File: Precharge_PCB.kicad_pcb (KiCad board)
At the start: 4 copper layers, 0 parts

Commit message: pcb: Setup net classes and import components
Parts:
- added C1: 22u, Capacitor_SMD:CP_Elec_6.3x7.7, F.Cu at (120.5, 110.7)
- added C10: 30p, Capacitor_SMD:C_0603_1608Metric, F.Cu at (76.6, 96.6)
- added C11: 100n, Capacitor_SMD:C_0603_1608Metric, F.Cu at (76.6, 99.1)
- added C12: 1u, Capacitor_SMD:C_0603_1608Metric, F.Cu at (76.6, 101.6)
- added C13: 100p, Capacitor_SMD:C_0603_1608Metric, F.Cu at (76.6, 104.1)
- added C14: 100p, Capacitor_SMD:C_0603_1608Metric, F.Cu at (76.6, 106.6)
- added C15: 1u, Capacitor_SMD:C_0603_1608Metric, F.Cu at (131.7, 124.9)
- added C16: 1u, Capacitor_SMD:C_0603_1608Metric, F.Cu at (131.7, 127.4)
- added C17: 1u, Capacitor_SMD:C_0603_1608Metric, F.Cu at (99.1, 118.7)
- added C18: 100n, Capacitor_SMD:C_0603_1608Metric, F.Cu at (99.1, 121.2)
- added C19: 1u, Capacitor_SMD:C_0603_1608Metric, F.Cu at (99.1, 123.7)
- added C2: 1u, Capacitor_SMD:C_0603_1608Metric, F.Cu at (72.6, 96.6)
- added C20: 100n, Capacitor_SMD:C_0603_1608Metric, F.Cu at (99.1, 126.2)
- added C21: 330p, Capacitor_SMD:C_0603_1608Metric, F.Cu at (99.1, 128.7)
- added C22: 330p, Capacitor_SMD:C_0603_1608Metric, F.Cu at (103.1, 118.7)
- added C23: 1u, Capacitor_SMD:C_0603_1608Metric, F.Cu at (103.1, 121.2)
- added C24: 1u, Capacitor_SMD:C_0603_1608Metric, F.Cu at (117.5, 118.7)
- added C25: 100n, Capacitor_SMD:C_0603_1608Metric, F.Cu at (117.5, 121.2)
- added C26: 1u, Capacitor_SMD:C_0603_1608Metric, F.Cu at (117.5, 123.7)
- added C27: 100n, Capacitor_SMD:C_0603_1608Metric, F.Cu at (117.5, 126.2)
- added C28: 330p, Capacitor_SMD:C_0603_1608Metric, F.Cu at (117.5, 128.7)
- added C29: 330p, Capacitor_SMD:C_0603_1608Metric, F.Cu at (121.5, 118.7)
- added C3: 1u, Capacitor_SMD:C_0603_1608Metric, F.Cu at (72.6, 99.1)
- added C30: 1u, Capacitor_SMD:C_0603_1608Metric, F.Cu at (121.5, 121.2)
- added C4: 1u, Capacitor_SMD:C_0603_1608Metric, F.Cu at (72.6, 101.6)
- added C5: 1u, Capacitor_SMD:C_0603_1608Metric, F.Cu at (72.6, 104.1)
- added C6: 1u, Capacitor_SMD:C_0603_1608Metric, F.Cu at (72.6, 106.6)
- added C7: 1u, Capacitor_SMD:C_0603_1608Metric, F.Cu at (72.6, 109.1)
- added C8: 1u, Capacitor_SMD:C_0603_1608Metric, F.Cu at (72.6, 111.6)
- added C9: 30p, Capacitor_SMD:C_0603_1608Metric, F.Cu at (72.6, 114.1)
- added D1: LED_Small, LED_SMD:LED_0603_1608Metric, F.Cu at (109.0, 64.9)
- added D10: LED_Small, LED_SMD:LED_0603_1608Metric, F.Cu at (113.1, 64.9)
- added D11: LED_Small, LED_SMD:LED_0603_1608Metric, F.Cu at (113.1, 67.5)
- added D12: LED_Small, LED_SMD:LED_0603_1608Metric, F.Cu at (113.1, 70.1)
- added D13: LED_Small, LED_SMD:LED_0603_1608Metric, F.Cu at (113.1, 72.7)
- added D14: LED_Small, LED_SMD:LED_0603_1608Metric, F.Cu at (113.1, 75.3)
- added D15: PESD2CAN, Package_TO_SOT_SMD:SOT-23, F.Cu at (93.4, 97.5)
- added D16: 1N4007, Diode_SMD:D_SMA, F.Cu at (103.0, 70.5)
- added D17: 1N4007, Diode_SMD:D_SMA, F.Cu at (103.0, 75.0)
- added D18: 3V6, Diode_SMD:D_SOD-323, F.Cu at (98.0, 112.2)
- added D19: 1N4007, Diode_SMD:D_SMA, F.Cu at (74.6, 132.4)
- added D2: SMAJ24CA, Diode_SMD:D_SMA, F.Cu at (103.0, 65.9)
- added D20: 1N4007, Diode_SMD:D_SMA, F.Cu at (159.0, 128.9)
- added D21: 1N4007, Diode_SMD:D_SMA, F.Cu at (133.8, 105.0)
- added D22: 1N4007, Diode_SMD:D_SMA, F.Cu at (133.8, 109.6)
- added D3: D_Schottky, Diode_SMD:D_SOD-323, F.Cu at (98.0, 103.4)
- added D4: D_Schottky, Diode_SMD:D_SOD-323, F.Cu at (98.0, 106.3)
- added D5: D_Schottky, Diode_SMD:D_SOD-323, F.Cu at (98.0, 109.3)
- added D6: LED_Small, LED_SMD:LED_0603_1608Metric, F.Cu at (109.0, 67.5)
- added D7: LED_Small, LED_SMD:LED_0603_1608Metric, F.Cu at (109.0, 70.1)
- added D8: LED_Small, LED_SMD:LED_0603_1608Metric, F.Cu at (109.0, 72.7)
- added D9: LED_Small, LED_SMD:LED_0603_1608Metric, F.Cu at (109.0, 75.3)
- added F1: Polyfuse, Capacitor_SMD:C_0805_2012Metric, F.Cu at (93.2, 113.7)
- added H1: MountingHole, MountingHole:MountingHole_3.2mm_M3, F.Cu at (111.3, 86.5)
- added H2: MountingHole, MountingHole:MountingHole_3.2mm_M3, F.Cu at (111.3, 94.5)
- added H3: MountingHole, MountingHole:MountingHole_3.2mm_M3, F.Cu at (111.3, 102.4)
- added H4: MountingHole, MountingHole:MountingHole_3.2mm_M3, F.Cu at (111.3, 110.4)
- added J1: Conn_01x02, yfs:MolexMicrofitPlus1x2, F.Cu at (76.3, 85.6)
- added J2: Conn_01x02, yfs:MolexMicrofitPlus1x2, F.Cu at (85.5, 85.6)
- added J3: Conn_01x02, yfs:MolexMicrofitPlus1x2, F.Cu at (94.7, 85.6)
- added J4: Conn_01x02, yfs:MolexMicrofitPlus1x2, F.Cu at (103.9, 85.6)
- added J5: Conn_01x08, yfs:MolexMicrofitPlus1x8, F.Cu at (122.7, 53.9)
- added J6: Conn_01x03, yfs:MolexMicrofitPlus1x3, F.Cu at (124.1, 85.6)
- added J7: Conn_01x04, yfs:MolexMicrofitPlus1x4, F.Cu at (82.3, 120.4)
- added J8: Conn_01x04, yfs:MolexMicrofitPlus1x4, F.Cu at (166.7, 116.9)
- added J9: Conn_01x06, yfs:IDC-Connector-2x3, F.Cu at (120.6, 75.9)
- added JP1: SolderJumper_2_Open, Jumper:SolderJumper-2_P1.3mm_Open_TrianglePad1.0x1.5mm, F.Cu at (93.1, 110.4)
- added K1: G2RL-1A, Relay_THT:Relay_SPST_Omron_G2RL-1A, F.Cu at (74.0, 55.3)
- added K2: G2RL-1A, Relay_THT:Relay_SPST_Omron_G2RL-1A, F.Cu at (88.1, 55.3)
- added K3: G9KB-1A, yfs:G9KB-1A, F.Cu at (145.3, 61.5)
- added K4: SPU01M-05, yfs:SPU01M-5, F.Cu at (149.9, 131.1)
- added Q1: DMN61D8LQ, Package_TO_SOT_SMD:SOT-23, F.Cu at (93.4, 102.0)
- added Q2: DMN61D8LQ, Package_TO_SOT_SMD:SOT-23, F.Cu at (93.4, 106.4)
- added Q3: DMN61D8LQ, Package_TO_SOT_SMD:SOT-23, F.Cu at (88.2, 119.6)
- added Q4: DMN61D8LQ, Package_TO_SOT_SMD:SOT-23, F.Cu at (88.2, 124.1)
- added Q5: DMN61D8LQ, Package_TO_SOT_SMD:SOT-23, F.Cu at (172.6, 116.1)
- added Q6: DMN61D8LQ, Package_TO_SOT_SMD:SOT-23, F.Cu at (172.6, 120.5)
- added Q7: DMN61D8LQ, Package_TO_SOT_SMD:SOT-23, F.Cu at (140.3, 105.0)
- added Q8: DMN61D8LQ, Package_TO_SOT_SMD:SOT-23, F.Cu at (140.3, 109.4)
- added R1: 10k, Resistor_SMD:R_0603_1608Metric, F.Cu at (76.6, 109.1)
- added R10: 330, Resistor_SMD:R_0603_1608Metric, F.Cu at (80.6, 111.6)
- added R11: 120, Resistor_SMD:R_0603_1608Metric, F.Cu at (80.6, 114.1)
- added R12: 10k, Resistor_SMD:R_0603_1608Metric, F.Cu at (84.6, 96.6)
- added R13: 10k, Resistor_SMD:R_0603_1608Metric, F.Cu at (84.6, 99.1)
- added R14: 43k, Resistor_SMD:R_0603_1608Metric, F.Cu at (84.6, 101.6)
- added R15: 10k, Resistor_SMD:R_0603_1608Metric, F.Cu at (84.6, 104.1)
- added R16: 10k, Resistor_SMD:R_0603_1608Metric, F.Cu at (87.8, 127.5)
- added R17: 10k, Resistor_SMD:R_0603_1608Metric, F.Cu at (87.8, 130.1)
- added R18: 10k, Resistor_SMD:R_0603_1608Metric, F.Cu at (172.2, 124.0)
- added R19: 10k, Resistor_SMD:R_0603_1608Metric, F.Cu at (172.2, 126.5)
- added R2: 330, Resistor_SMD:R_0603_1608Metric, F.Cu at (76.6, 111.6)
- added R20: 10k, Resistor_SMD:R_0603_1608Metric, F.Cu at (144.7, 104.0)
- added R21: 1k, yfs:APLR1000, F.Cu at (142.8, 41.5)
- added R22: R, Resistor_SMD:R_0603_1608Metric, F.Cu at (131.7, 129.9)
- added R23: R, Resistor_SMD:R_0603_1608Metric, F.Cu at (131.7, 132.4)
- added R24: 1k, Resistor_SMD:R_0603_1608Metric, F.Cu at (131.7, 134.9)
- added R25: 200k, Resistor_SMD:R_0603_1608Metric, F.Cu at (131.7, 137.4)
- added R26: 10k, Resistor_SMD:R_0603_1608Metric, F.Cu at (131.7, 139.9)
- added R27: 750k, Resistor_SMD:R_0805_2012Metric, F.Cu at (94.9, 118.9)
- added R28: 750k, Resistor_SMD:R_0805_2012Metric, F.Cu at (94.9, 121.8)
- added R29: 750k, Resistor_SMD:R_0805_2012Metric, F.Cu at (94.9, 124.8)
- added R3: 330, Resistor_SMD:R_0603_1608Metric, F.Cu at (76.6, 114.1)
- added R30: 750k, Resistor_SMD:R_0805_2012Metric, F.Cu at (94.9, 127.7)
- added R31: 750k, Resistor_SMD:R_0805_2012Metric, F.Cu at (94.9, 130.7)
- added R32: 750k, Resistor_SMD:R_0805_2012Metric, F.Cu at (94.9, 133.6)
- added R33: 47k, Resistor_SMD:R_0805_2012Metric, F.Cu at (94.9, 136.6)
- added R34: 3k3, Resistor_SMD:R_0603_1608Metric, F.Cu at (103.1, 123.7)
- added R35: 3k3, Resistor_SMD:R_0603_1608Metric, F.Cu at (103.1, 126.2)
- added R36: 3k3, Resistor_SMD:R_0603_1608Metric, F.Cu at (103.1, 128.7)
- added R37: 3k3, Resistor_SMD:R_0603_1608Metric, F.Cu at (107.1, 118.7)
- added R38: 10k, Resistor_SMD:R_0603_1608Metric, F.Cu at (107.1, 121.2)
- added R39: 10k, Resistor_SMD:R_0603_1608Metric, F.Cu at (107.1, 123.7)
- added R4: 330, Resistor_SMD:R_0603_1608Metric, F.Cu at (80.6, 96.6)
- added R40: 750k, Resistor_SMD:R_0805_2012Metric, F.Cu at (113.3, 118.9)
- added R41: 750k, Resistor_SMD:R_0805_2012Metric, F.Cu at (113.3, 121.8)
- added R42: 750k, Resistor_SMD:R_0805_2012Metric, F.Cu at (113.3, 124.8)
- added R43: 750k, Resistor_SMD:R_0805_2012Metric, F.Cu at (113.3, 127.7)
- added R44: 750k, Resistor_SMD:R_0805_2012Metric, F.Cu at (113.3, 130.7)
- added R45: 750k, Resistor_SMD:R_0805_2012Metric, F.Cu at (113.3, 133.6)
- added R46: 47k, Resistor_SMD:R_0805_2012Metric, F.Cu at (113.3, 136.6)
- added R47: 3k3, Resistor_SMD:R_0603_1608Metric, F.Cu at (121.5, 123.7)
- added R48: 3k3, Resistor_SMD:R_0603_1608Metric, F.Cu at (121.5, 126.2)
- added R49: 3k3, Resistor_SMD:R_0603_1608Metric, F.Cu at (121.5, 128.7)
- added R5: 330, Resistor_SMD:R_0603_1608Metric, F.Cu at (80.6, 99.1)
- added R50: 3k3, Resistor_SMD:R_0603_1608Metric, F.Cu at (125.5, 118.7)
- added R51: 10k, Resistor_SMD:R_0603_1608Metric, F.Cu at (125.5, 121.2)
- added R52: 10k, Resistor_SMD:R_0603_1608Metric, F.Cu at (125.5, 123.7)
- added R6: 330, Resistor_SMD:R_0603_1608Metric, F.Cu at (80.6, 101.6)
- added R7: 330, Resistor_SMD:R_0603_1608Metric, F.Cu at (80.6, 104.1)
- added R8: 330, Resistor_SMD:R_0603_1608Metric, F.Cu at (80.6, 106.6)
- added R9: 330, Resistor_SMD:R_0603_1608Metric, F.Cu at (80.6, 109.1)
- added SW1: SW_Push, Button_Switch_SMD:SW_Push_1P1T_NO_Vertical_Wuerth_434133025816, F.Cu at (103.5, 110.4)
- added TP1: TestPoint, TestPoint:TestPoint_Keystone_5000-5004_Miniature, F.Cu at (88.8, 97.5)
- added TP2: TestPoint, TestPoint:TestPoint_Keystone_5000-5004_Miniature, F.Cu at (88.8, 101.8)
- added TP3: TestPoint, TestPoint:TestPoint_Keystone_5000-5004_Miniature, F.Cu at (88.8, 106.2)
- added TP4: TestPoint, TestPoint:TestPoint_Keystone_5000-5004_Miniature, F.Cu at (88.8, 110.5)
- added U1: TPS7B88, Package_TO_SOT_SMD:TO-252-2, F.Cu at (122.0, 67.8)
- added U2: MCP1700x-330xxMB, Package_TO_SOT_SMD:SOT-89-3, F.Cu at (103.5, 105.0)
- added U3: STM32F103C8Tx, Package_QFP:LQFP-48_7x7mm_P0.5mm, F.Cu at (121.0, 101.0)
- added U4: SN65HVD1050D, Package_SO:SOIC-8_3.9x4.9mm_P1.27mm, F.Cu at (100.1, 98.7)
- added U5: LM393, Package_SO:SOIC-8_3.9x4.9mm_P1.27mm, F.Cu at (138.0, 127.0)
- added U6: 4N35, Package_DIP:DIP-6_W7.62mm, F.Cu at (143.8, 125.7)
- added U7: AMC1351, Package_SO:SOIC-8_3.9x4.9mm_P1.27mm, F.Cu at (101.3, 133.3)
- added U8: AMC1351, Package_SO:SOIC-8_3.9x4.9mm_P1.27mm, F.Cu at (119.7, 133.3)
- added U9: TLV6002, Package_SO:SOIC-8_3.9x4.9mm_P1.27mm, F.Cu at (138.0, 133.6)
- added Y1: 8M, Crystal:Crystal_SMD_5032-2Pin_5.0x3.2mm, F.Cu at (110.7, 79.2)

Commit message: Revision A
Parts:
- added C31: 1u, Capacitor_SMD:C_0603_1608Metric, F.Cu at (103.5, 68.0)
- added F2: Polyfuse, Capacitor_SMD:C_0805_2012Metric, F.Cu at (101.5, 114.2)
- added G***: LOGO, LOGO, F.Cu at (224.0, 69.0)
- added G***: LOGO, LOGO, F.Cu at (125.0, 100.0)
- added G***: LOGO, MyLibrary:Logo, F.Cu at (196.9, 124.7)
- added G***: LOGO, MyLibrary:Logo, B.Cu at (139.4, 125.8)
- added G***: LOGO, LOGO, B.Cu at (208.4, 124.0)
- added G***: LOGO, LOGO, B.Cu at (224.0, 69.0)
- added kibuzzard-6910BB45: G***, kibuzzard-6910BB45, F.Cu at (83.0, 62.0)
- added kibuzzard-6910BB76: G***, kibuzzard-6910BB76, F.Cu at (122.0, 82.2)
- added kibuzzard-694056F2: G***, kibuzzard-694056F2, F.Cu at (70.5, 41.9)
- added kibuzzard-694056F9: G***, kibuzzard-694056F9, F.Cu at (70.5, 50.9)
- added kibuzzard-69405726: G***, kibuzzard-69405726, F.Cu at (132.0, 36.2)
- added kibuzzard-69405880: G***, kibuzzard-69405880, F.Cu at (70.5, 59.9)
- added kibuzzard-694058AC: G***, kibuzzard-694058AC, F.Cu at (70.5, 84.0)
- added kibuzzard-694058D8: G***, kibuzzard-694058D8, F.Cu at (70.5, 69.0)
- added kibuzzard-69405918: G***, kibuzzard-69405918, F.Cu at (65.0, 100.5)
- added kibuzzard-69408760: G***, kibuzzard-69408760, F.Cu at (231.5, 53.0)
- added kibuzzard-6940937D: G***, kibuzzard-6940937D, F.Cu at (96.0, 115.2)
- K3: value G9KB-1A -> G9EJH-1-E; footprint yfs:G9KB-1A -> yfs:G9EJH-1-E
- R27, R28, R29, R30, R31, R32, R33, R40, R41, R42, R43, R44, R45, R46: footprint Resistor_SMD:R_0805_2012Metric -> Resistor_SMD:R_1206_3216Metric
- moved H3 137.7 mm to (232.0, 36.0)
- moved R27 129.8 mm to (219.0, 81.0), turned to -90 degrees
- moved R28 129.1 mm to (219.0, 86.5), turned to -90 degrees
- moved R29 128.4 mm to (219.0, 92.0), turned to -90 degrees
- moved R30 127.8 mm to (219.0, 97.5), turned to -90 degrees
- moved R31 127.2 mm to (219.0, 103.0), turned to -90 degrees
- moved R32 126.6 mm to (219.0, 108.5), turned to -90 degrees
- moved R33 126.2 mm to (219.0, 114.0), turned to -90 degrees
- moved H4 121.7 mm to (232.0, 126.4)
- moved R40 120.8 mm to (228.0, 81.0), turned to -90 degrees
- moved R41 120.0 mm to (228.0, 86.5), turned to -90 degrees
- moved R42 119.3 mm to (228.0, 92.0), turned to -90 degrees
- moved R43 118.6 mm to (228.0, 97.5), turned to -90 degrees
- moved R44 118.0 mm to (228.0, 103.0), turned to -90 degrees
- moved R45 117.4 mm to (228.0, 108.5), turned to -90 degrees
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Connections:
- D6 pad 1: Net-(D6-K) -> GND
- D6 pad 2: /STATUS LED -> Net-(D6-A)
- J5 pad 2: +5VL -> Net-(J5-Pin_2)
- R2 pad 1: GND -> Net-(D6-A)
- R2 pad 2: Net-(D6-K) -> /STATUS LED
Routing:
- net GND1: track 0.00 -> 249.7 mm, vias 0 -> 4
- net SHUTDOWN_FINAL: track 0.00 -> 224.6 mm, vias 0 -> 1
- net +3V3: track 0.00 -> 202.4 mm, vias 0 -> 48
- net PRECHARGE_ACT: track 0.00 -> 170.3 mm
- net +5VL: track 0.00 -> 149.3 mm, vias 0 -> 2
- net PRECHARGE_INT: track 0.00 -> 99.5 mm, vias 0 -> 1
- net AIR-_ACT: track 0.00 -> 96.3 mm, vias 0 -> 2
- net AIR+_ACT: track 0.00 -> 93.1 mm, vias 0 -> 4
- net AIR-_CMD: track 0.00 -> 87.1 mm, vias 0 -> 2
- net /HV Sampling/Tractive System: track 0.00 -> 85.0 mm, vias 0 -> 4
- net SHUTDOWN_IN: track 0.00 -> 79.3 mm
- net PRECHARGE_CMD: track 0.00 -> 76.0 mm, vias 0 -> 2
- net +5VA: track 0.00 -> 74.2 mm
- net /HV Sampling/Accumulator: track 0.00 -> 67.6 mm, vias 0 -> 4
- net /NRST: track 0.00 -> 65.8 mm, vias 0 -> 2
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- added copper zone on B.Cu, net +12V
- added copper zone on F.Cu, net +12V
- added copper zone on B.Cu, net +3V3
- added copper zone on F.Cu, net +3V3
- added copper zone on F.Cu, net +5V
- added copper zone on B.Cu, net GND
- added copper zone on F.Cu, net GND
- added copper zone on F.Cu, net Net-(D2-A2)
- added copper zone on F.Cu, net Net-(D3-K)
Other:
- board outline added: 180 x 100.4 mm
- copper layers 4 -> 2
- board text added: "+5VL"
- board text added: "3.00mm"
- board text added: "A+"
- board text added: "A-"
- board text added: "ACC+"
- board text added: "AIR+"
- board text added: "AIR+_ACT"
- board text added: "AIR+_INT"
- board text added: "AIR-"
- board text added: "AIR-_ACT"
- board text added: "AIR-_INT"
- board text added: "B+"
- board text added: "B-"
- board text added: "Bridge to remove"
- board text added: "DISCHARGE"
- board text added: "DISCONNECT"
- board text added: "Dec 2025"
- board text added: "H"
- board text added: "HIGH VOLTAGE"
- board text added: "L"
- board text added: "LOGAN CAREY"
- board text added: "LV+"
- board text added: "LV-"
- board text added: "LVS"
- board text added: "Manufactured By"
- board text added: "OWEN SMITH"
- board text added: "PRECHARGE"
- board text added: "PREC_ACT"
- board text added: "PREC_INT"
- board text added: "Rev A"
- board text added: "SDN"
- board text added: "STATE 1"
- board text added: "STATE 2"
- board text added: "STATE 3"
- board text added: "STATE 4"
- board text added: "TS"
- board text added: "TS+"
- board text added: "TS-"
- board text added: "TSAL"
- board text added: "TSAL +5VL Check"

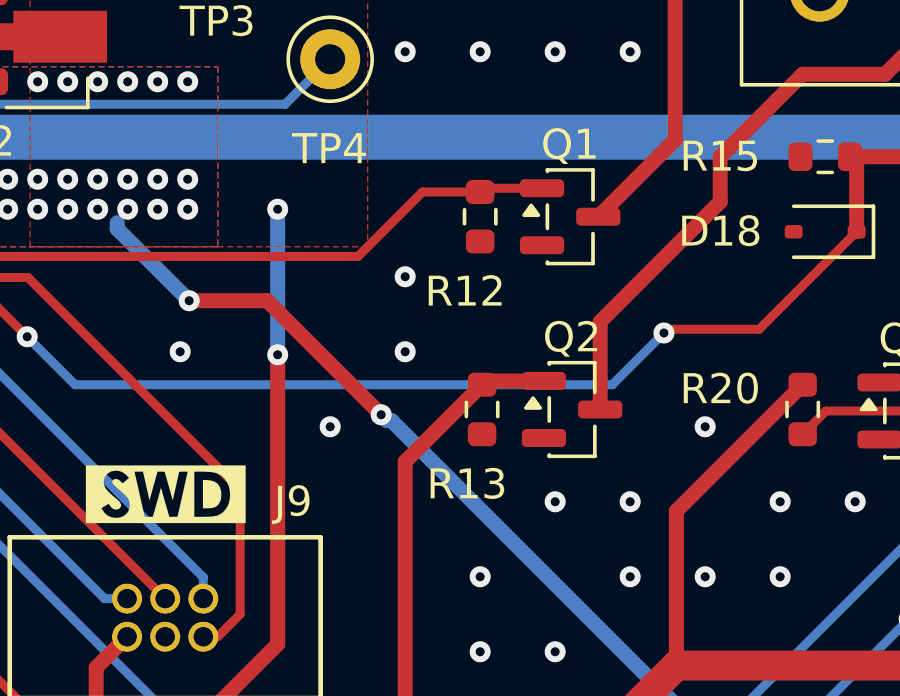
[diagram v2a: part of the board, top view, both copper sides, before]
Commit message: *: Remove unnecessary MOSFET pull-downs
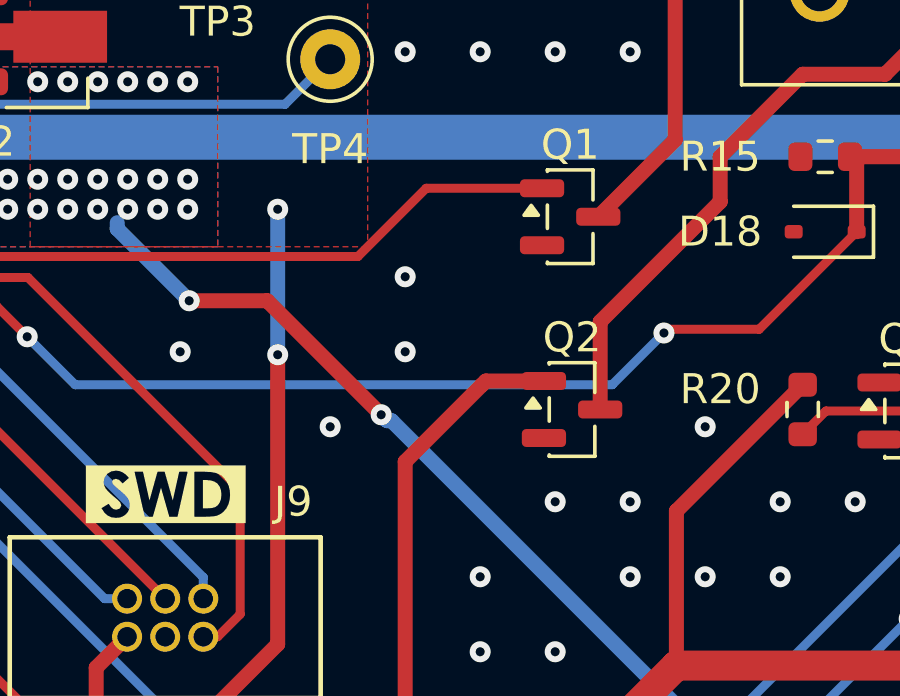
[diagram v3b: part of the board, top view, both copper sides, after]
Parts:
- removed R12, R13: 10k, Resistor_SMD:R_0603_1608Metric

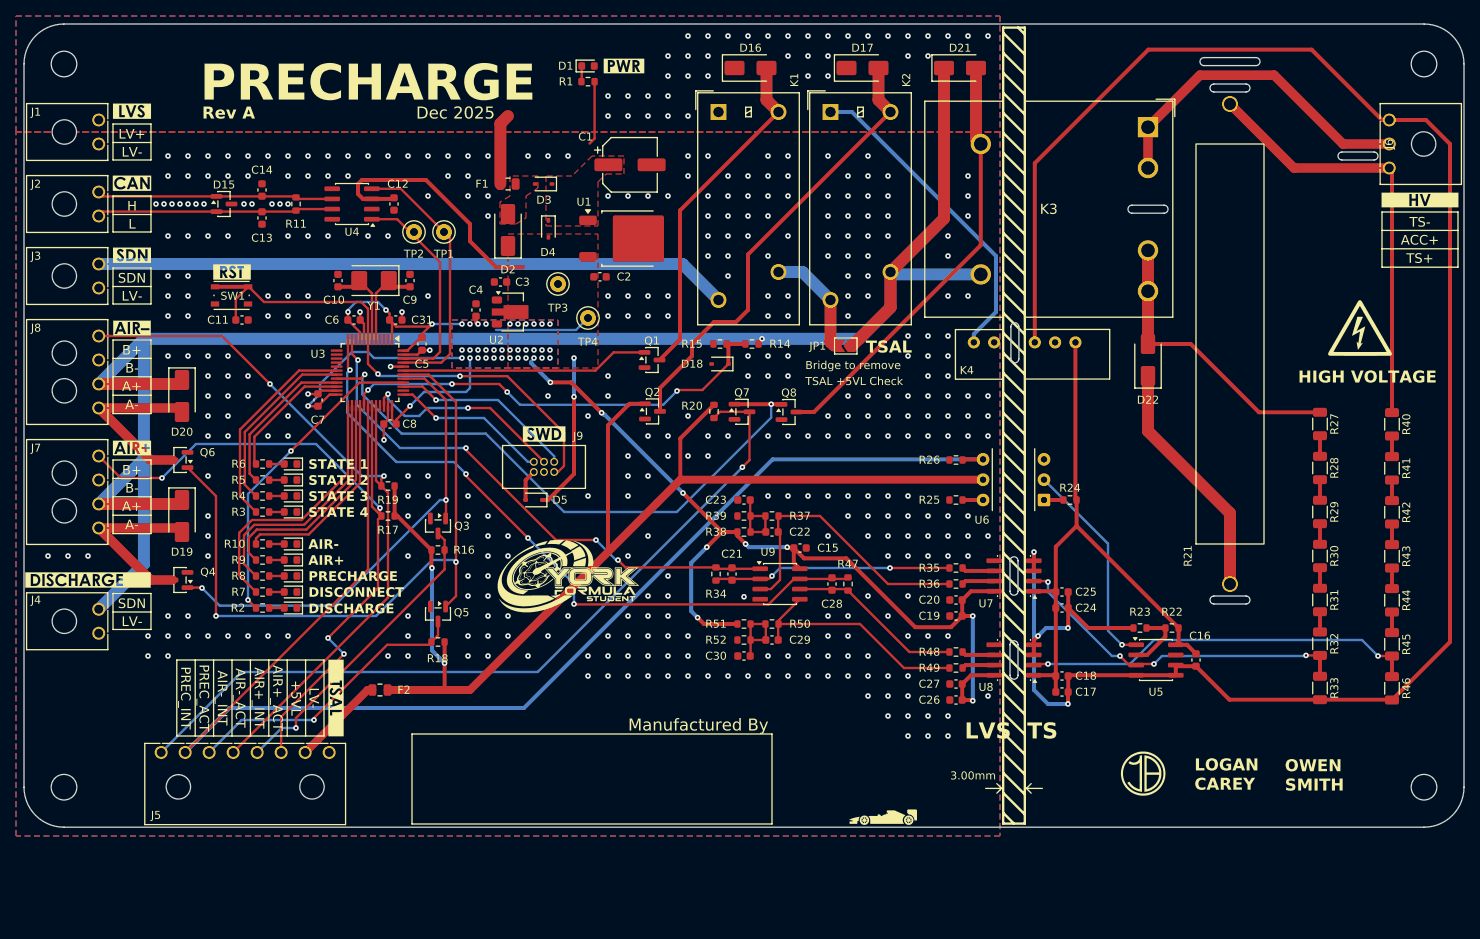
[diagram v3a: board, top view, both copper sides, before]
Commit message: Updated layout
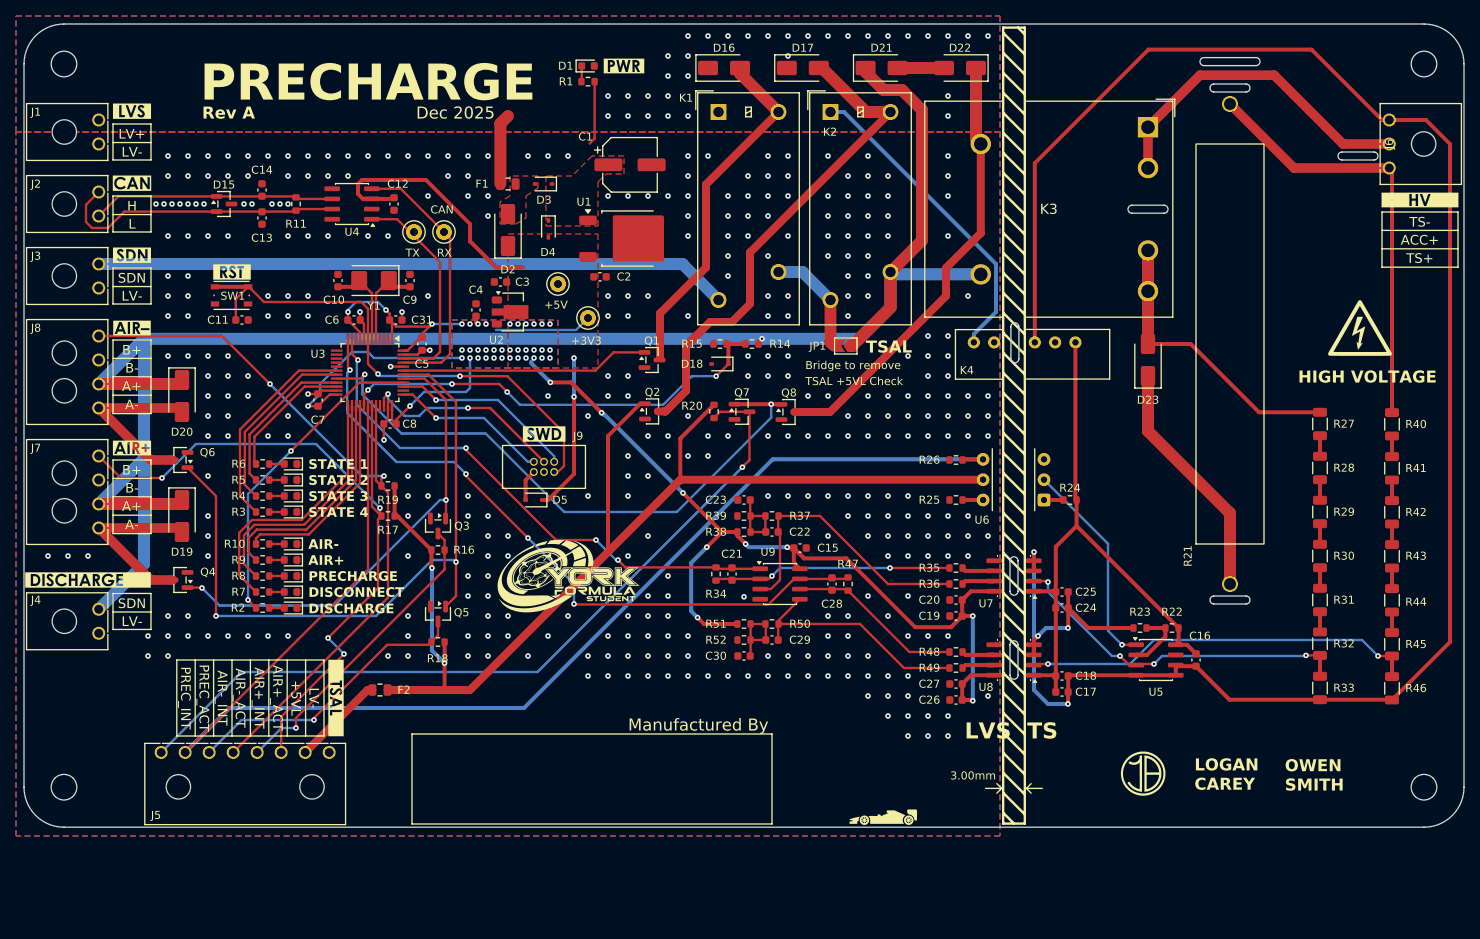
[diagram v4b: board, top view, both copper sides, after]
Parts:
- added D22: 24V, Diode_SMD:D_SMA, F.Cu at (174.0, 36.5)
- moved D21 9.80 mm to (164.2, 36.5)
- moved D17 7.46 mm to (154.3, 36.5)
- moved D16 3.31 mm to (144.5, 36.5)
- renumbered D22 to D23
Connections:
- J2 pad 1: CANH -> CANL
- J2 pad 2: CANL -> CANH
- K3 pad 2: Net-(D21-A) -> Net-(D22-K)
- Q8 pad 3: Net-(D21-A) -> Net-(D22-K)
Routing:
- net Net-(D22-K): track 0.00 -> 55.5 mm
- net Net-(D21-A): track 54.1 -> 5.80 mm
- net CANH: track 29.5 -> 36.5 mm
- net Net-(D17-A): track 57.1 -> 63.0 mm
- net SHUTDOWN_FINAL: track 224.6 -> 227.7 mm
- net Net-(D16-A): track 43.3 -> 44.4 mm
- net CANL: track 29.5 -> 30.3 mm
- net +5VL: track 149.3 -> 148.5 mm
- net +12V: track 49.0 -> 48.4 mm, vias 38 -> 32
- net GND: vias 370 -> 365
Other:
- board text added: "+3V3"
- board text added: "+5V"
- board text added: "CAN"
- board text added: "RX"
- board text added: "TX"
